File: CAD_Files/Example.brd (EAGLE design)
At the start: 86 x 54 mm, 9 parts, among them IC1 LM555D, Q1 BSS806N

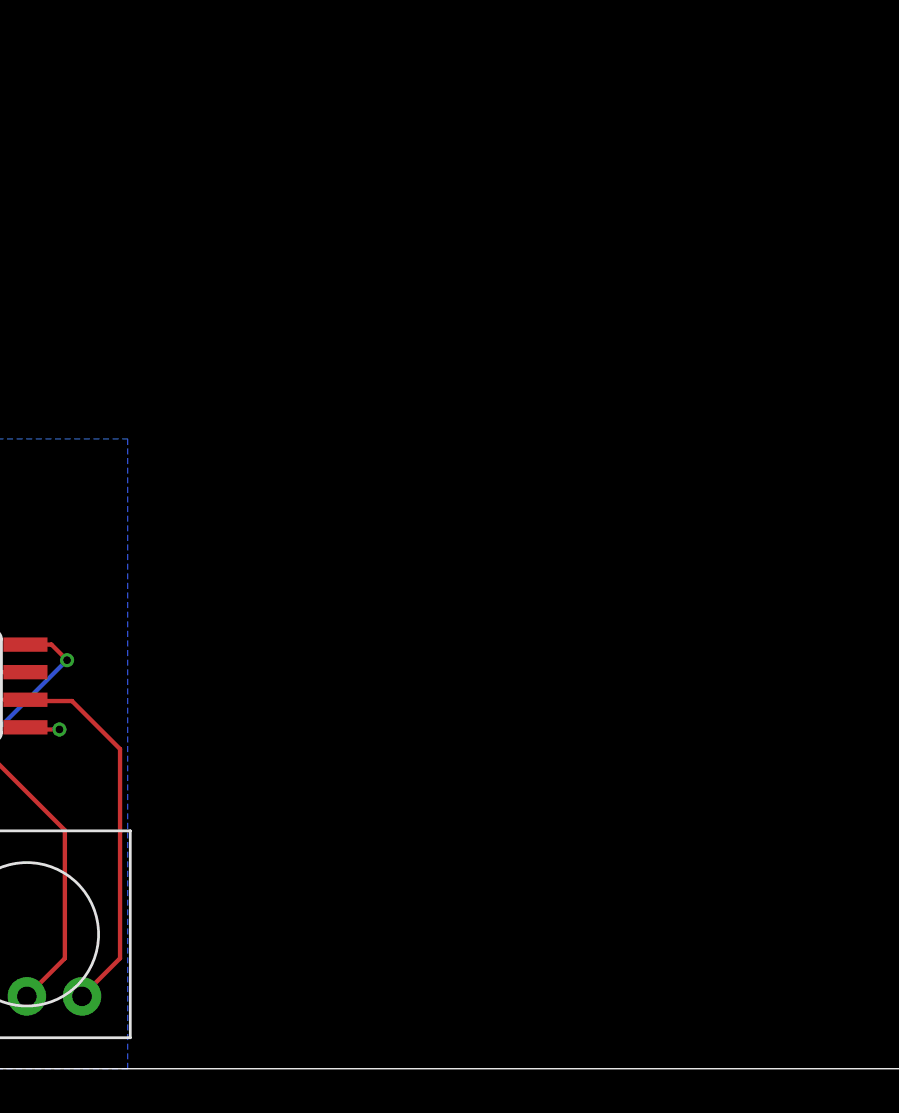
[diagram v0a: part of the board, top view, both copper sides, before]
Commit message: Added picture and silkscreen
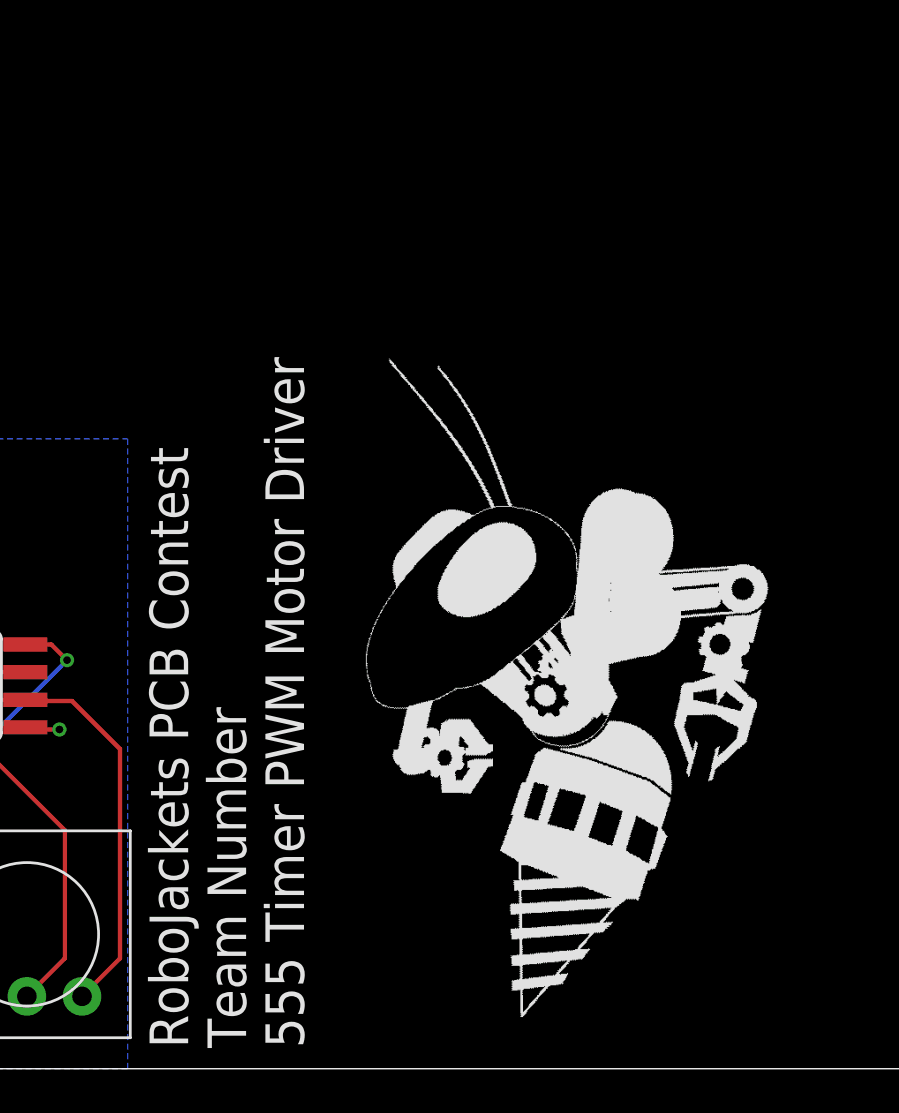
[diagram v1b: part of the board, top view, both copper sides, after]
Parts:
- added U$2: (no value), RoboJackets-Aesthetics:ROBOBUZZ_1.4X
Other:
- board text added: "RoboJackets PCB Contest Team Number 555 Timer PWM Motor Driver"
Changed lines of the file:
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@@
 <setting verticaltext="up"/>
 </settings>
-<grid distance="1" unitdist="mm" unit="mm" style="lines" multiple="1" display="no" altdistance="0.01" altunitdist="mm" altunit="mm"/>
+<grid distance="0.01" unitdist="mm" unit="mm" style="lines" multiple="1" display="no" altdistance="0.01" altunitdist="mm" altunit="mm"/>
 <layers>
 <layer number="1" name="Top" color="4" fill="1" visible="yes" active="yes"/>
@@
 <wire x1="0" y1="54" x2="0" y2="0" width="0" layer="20"/>
 <text x="2.13" y="28.48" size="2.5" layer="21" rot="SR270">ON</text>
+<text x="33.12" y="0.96" size="1.778" layer="21" rot="R90">RoboJackets PCB Contest
+Team Number
+555 Timer PWM Motor Driver</text>
 </plain>
 <attributes>
@@
 </element>
 <element name="U$1" library="Example" package="MFS101D-6-Z" value="MFS101D-6-Z" x="4.91" y="17.97" smashed="yes" rot="R90"/>
+<element name="U$2" library="RoboJackets-Aesthetics" package="ROBOBUZZ_1.4X" value="" x="43.06" y="2.36" smashed="yes"/>
 </elements>
 <signals>
@@
 </signals>
 <mfgpreviewcolors>
-<mfgpreviewcolor name="soldermaskcolor" color="0xC8008000"/>
+<mfgpreviewcolor name="soldermaskcolor" color="0xC8000000"/>
 <mfgpreviewcolor name="silkscreencolor" color="0xFFFEFEFE"/>
 <mfgpreviewcolor name="backgroundcolor" color="0xFF282828"/>
@@
 </drawing>
 <compatibility>
+<note version="6.3" minversion="6.2.2" severity="warning">
+Since Version 6.2.2 text objects can contain more than one line,
+which will not be processed correctly with this version.
+</note>
 <note version="8.2" severity="warning">
 Since Version 8.2, EAGLE supports online libraries. The ids

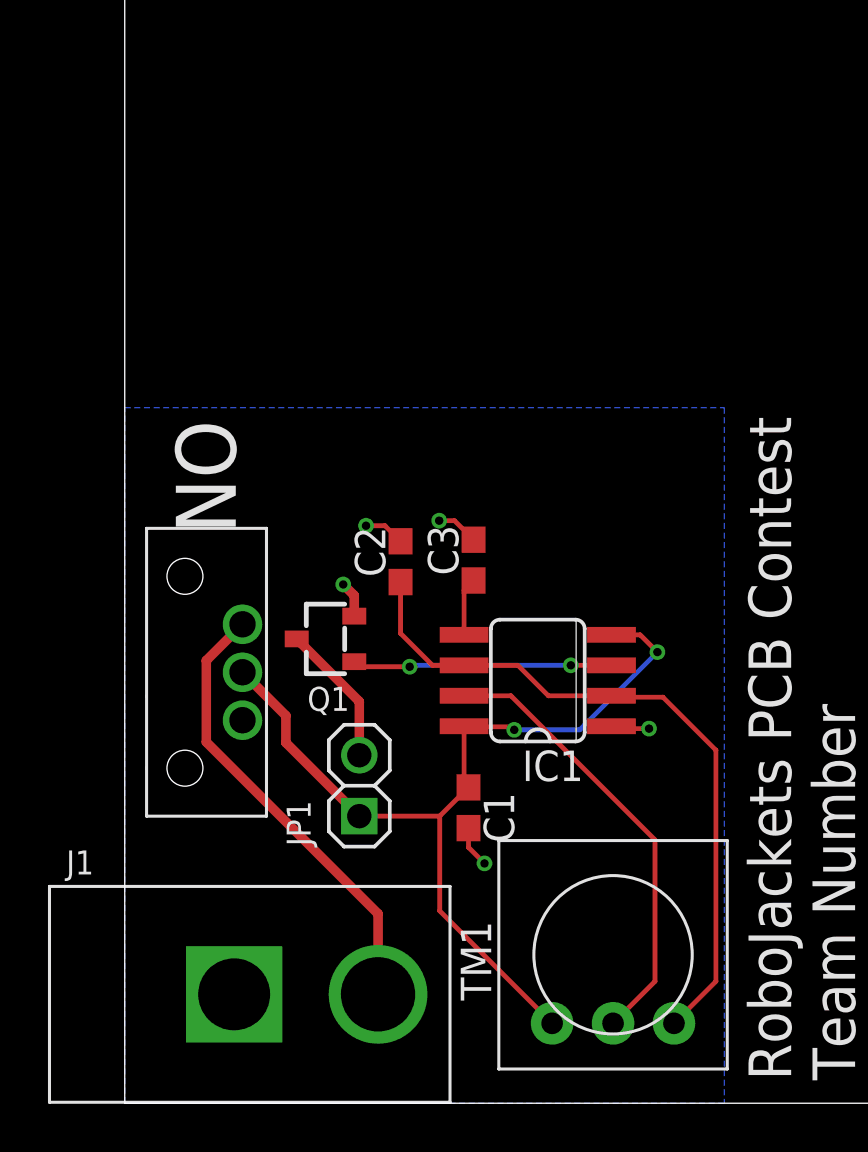
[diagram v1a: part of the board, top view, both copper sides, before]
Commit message: Added decoupling capacitors, fixed Library style guide compliance
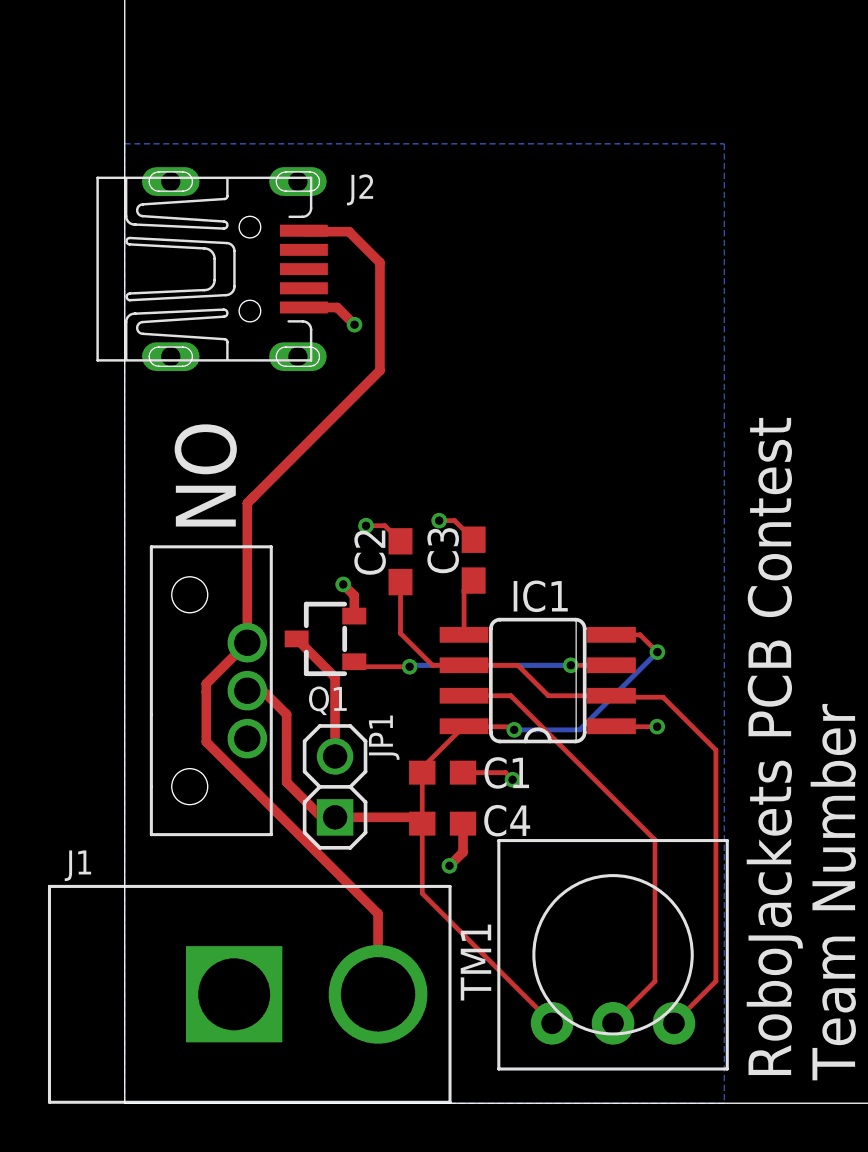
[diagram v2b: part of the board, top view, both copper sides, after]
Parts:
- removed U$1: MFS101D-6-Z, Example:MFS101D-6-Z
- added C4: 10uF, rcl:C0603
- added J2: UX60-MB-5S8, RoboJackets-Connectors:UX60-MB-5S8
- added SW1: MFS101D-6-Z, Example:MFS101D-6-Z
- moved C1 1.82 mm to (13.3, 13.8), turned to 0 degrees
- moved JP1 1.01 mm to (8.77, 13.2)
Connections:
- removed net N$4: J1.P$2, U$1.3
- new net N$5: J1.P$2, J2.1, SW1.3
- net +9V: now also C4.1, SW1.2; no longer U$1.2
- net GND: now also C4.2, J2.5
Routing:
- net N$5: track 0.00 -> 40.2 mm
- net N$4: track 19.0 -> 0.00 mm
- net GND: track 8.34 -> 13.5 mm, vias 5 -> 7

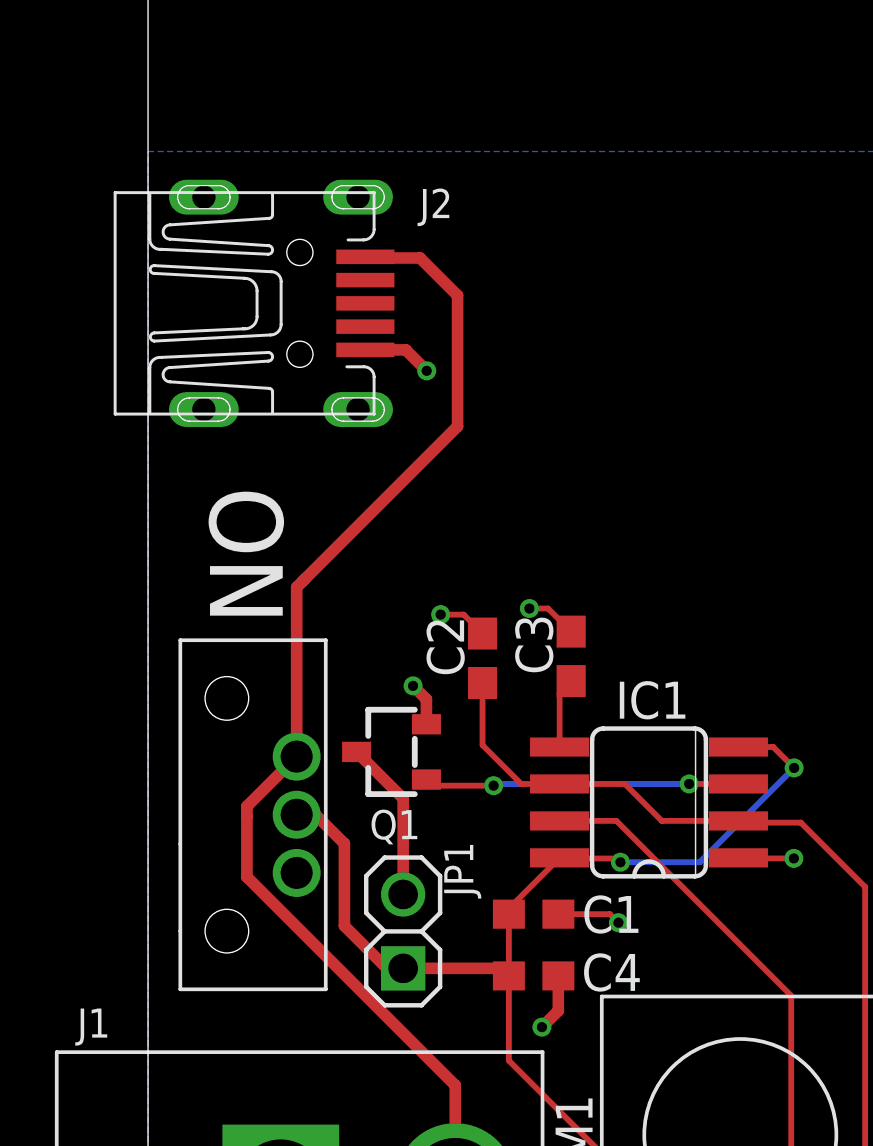
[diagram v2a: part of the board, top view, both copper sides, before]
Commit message: Library edits, power switching transistor, 3d CAD
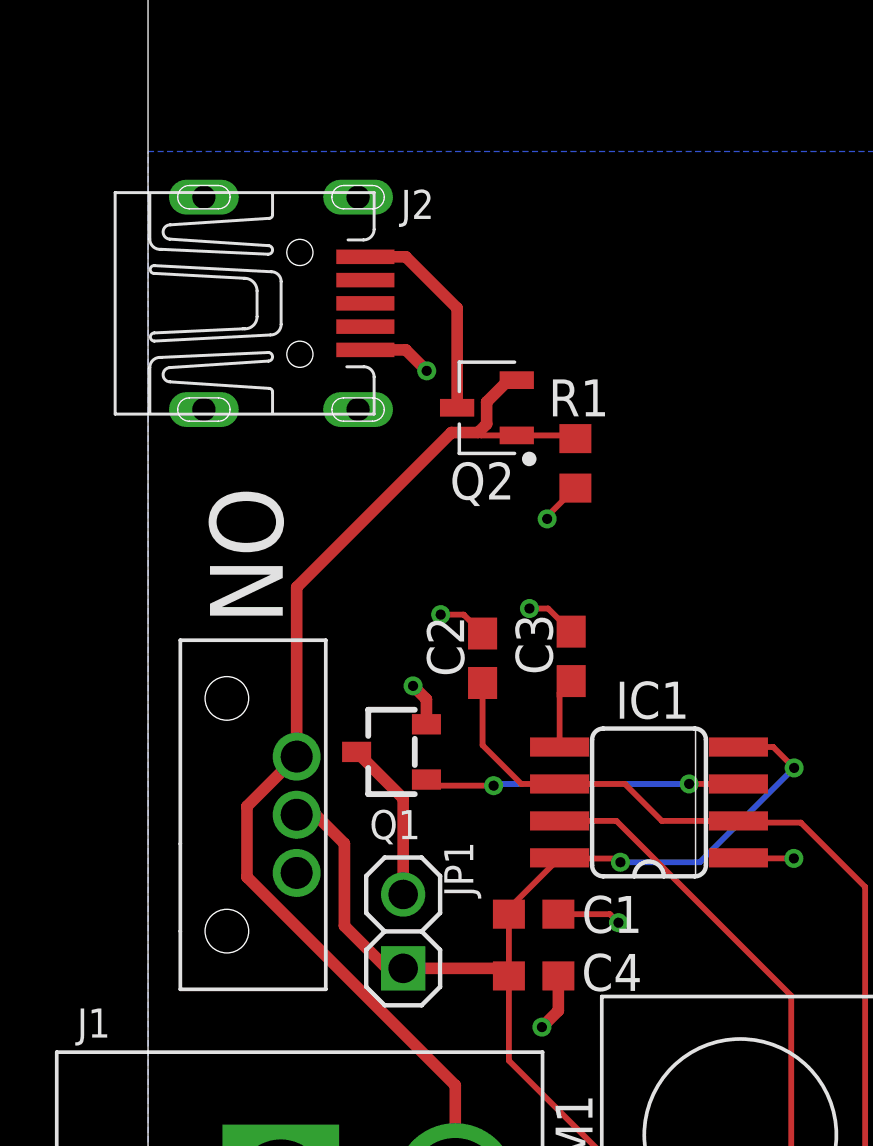
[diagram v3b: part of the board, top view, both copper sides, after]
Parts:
- added Q2: SSM3J356R, Example:SOT95P240X80-3N
- added R1: 10K, rcl:R0603
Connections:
- removed net N$5: J1.P$2, J2.1, SW1.3
- new net N$4: J2.1, Q2.3
- new net N$6: J1.P$2, Q2.1, Q2.2, R1.2, SW1.3
- net GND: now also R1.1
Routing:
- net N$5: track 40.2 -> 0.00 mm
- net N$6: track 0.00 -> 38.5 mm
- net N$4: track 0.00 -> 7.31 mm
- net GND: track 13.5 -> 14.9 mm, vias 7 -> 8
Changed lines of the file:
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@@
 <?xml version="1.0" encoding="utf-8"?>
 <!DOCTYPE eagle SYSTEM "eagle.dtd">
-<eagle version="9.5.2">
+<eagle version="9.6.2">
 <drawing>
 <settings>
@@
 <element name="J2" library="RoboJackets-Connectors" package="UX60-MB-5S8" value="UX60-MB-5S8" x="-1.18" y="34.78" smashed="yes">
 <attribute name="DKPN" value="H2960CT-ND" x="-1.18" y="34.78" size="1.778" layer="27" display="off"/>
-<attribute name="NAME" x="9.33" y="37.71" size="1" layer="25" font="vector"/>
-<attribute name="VALUE" x="-0.18" y="29.78" size="1" layer="27" font="vector" align="top-left"/>
+<attribute name="NAME" x="8.69" y="37.68" size="1" layer="25" font="vector"/>
 </element>
 <element name="C4" library="rcl" library_urn="urn:adsk.eagle:library:334" package="C0603" package3d_urn="urn:adsk.eagle:package:23616/2" value="10uF" x="13.255" y="11.66" smashed="yes">
@@
 <attribute name="SPICEPREFIX" value="C" x="13.255" y="11.66" size="1.778" layer="27" display="off"/>
 </element>
-<element name="SW1" library="Example" package="MFS101D-6-Z" value="MFS101D-6-Z" x="5.11" y="17.2" smashed="yes" rot="R90"/>
+<element name="SW1" library="Example" package="MFS101D-6-Z" value="MFS101D-6-Z" x="5.11" y="17.2" smashed="yes" rot="R90">
+<attribute name="DKPN" value="563-1555-ND" x="5.11" y="17.2" size="1.778" layer="27" rot="R90" display="off"/>
+</element>
+<element name="R1" library="rcl" library_urn="urn:adsk.eagle:library:334" package="R0603" package3d_urn="urn:adsk.eagle:package:23555/3" value="10K" x="14.69" y="29.28" smashed="yes" rot="R90">
+<attribute name="NAME" x="13.765" y="30.895" size="1.27" layer="25"/>
+<attribute name="POPULARITY" value="77" x="14.69" y="29.28" size="1.778" layer="27" rot="R90" display="off"/>
+<attribute name="SPICEPREFIX" value="R" x="14.69" y="29.28" size="1.778" layer="27" rot="R90" display="off"/>
+</element>
+<element name="Q2" library="Example" package="SOT95P240X80-3N" package3d_urn="urn:adsk.eagle:package:24993154/1" value="SSM3J356R" x="11.65" y="31.19" smashed="yes" rot="R180">
+<attribute name="NAME" x="11.49" y="29.3064" size="1.27" layer="25" rot="R180" align="bottom-center"/>
+</element>
 </elements>
 <signals>
@@
 <wire x1="15.877" y1="13.783" x2="16.17" y2="13.49" width="0.2" layer="1"/>
 <via x="16.17" y="13.49" extent="1-16" drill="0.35"/>
+<contactref element="R1" pad="1"/>
+<wire x1="14.69" y1="28.43" x2="13.72" y2="27.46" width="0.2" layer="1"/>
+<wire x1="13.72" y1="27.46" x2="13.72" y2="27.37" width="0.2" layer="1"/>
+<via x="13.72" y="27.37" extent="1-16" drill="0.35"/>
 </signal>
 <signal name="+9V">
@@
 <wire x1="16.239096875" y1="15.569096875" x2="16.11159375" y2="15.6966" width="0.2" layer="1"/>
 <wire x1="16.11159375" y1="15.6966" x2="14.17" y2="15.6966" width="0.2" layer="1"/>
-<wire x1="8.86" y1="12.01" x2="8.77" y2="11.92" width="0.2" layer="1"/>
 <contactref element="C4" pad="1"/>
 <contactref element="SW1" pad="2"/>
@@
 <wire x1="8.77" y1="17.76" x2="8.77" y2="14.46" width="0.4" layer="1"/>
 </signal>
-<signal name="N$5">
+<signal name="N$4">
 <contactref element="J2" pad="1"/>
+<contactref element="Q2" pad="3"/>
+<wire x1="7.47" y1="36.38" x2="8.86" y2="36.38" width="0.4" layer="1"/>
+<wire x1="10.6255" y1="34.6145" x2="10.6255" y2="31.19" width="0.4" layer="1"/>
+<wire x1="8.86" y1="36.38" x2="10.6255" y2="34.6145" width="0.4" layer="1"/>
+</signal>
+<signal name="N$6">
+<contactref element="R1" pad="2"/>
+<contactref element="Q2" pad="1"/>
+<wire x1="14.58" y1="30.24" x2="12.6745" y2="30.24" width="0.2" layer="1"/>
+<wire x1="14.58" y1="30.24" x2="14.69" y2="30.13" width="0.2" layer="1"/>
 <contactref element="J1" pad="P$2"/>
+<contactref element="SW1" pad="3"/>
+<contactref element="Q2" pad="2"/>
 <wire x1="10.562" y1="7.898" x2="10.562" y2="4.54" width="0.4" layer="1"/>
-<wire x1="3.4" y1="15.06" x2="3.4" y2="17.15" width="0.4" layer="1"/>
+<wire x1="3.4" y1="15.06" x2="3.4" y2="17.49" width="0.4" layer="1"/>
 <wire x1="10.562" y1="7.898" x2="3.4" y2="15.06" width="0.4" layer="1"/>
-<wire x1="7.47" y1="36.38" x2="7.51" y2="36.34" width="0.4" layer="1"/>
-<wire x1="7.51" y1="36.34" x2="9.35" y2="36.34" width="0.4" layer="1"/>
-<wire x1="9.35" y1="36.34" x2="10.64" y2="35.05" width="0.4" layer="1"/>
-<wire x1="10.64" y1="35.05" x2="10.64" y2="30.55" width="0.4" layer="1"/>
-<wire x1="10.64" y1="30.55" x2="5.395" y2="25.305" width="0.4" layer="1"/>
-<contactref element="SW1" pad="3"/>
-<wire x1="5.395" y1="25.305" x2="5.31" y2="25.22" width="0.4" layer="1"/>
 <wire x1="5.11" y1="19.2" x2="3.4" y2="17.49" width="0.4" layer="1"/>
-<wire x1="3.4" y1="17.49" x2="3.4" y2="17.15" width="0.4" layer="1"/>
 <wire x1="5.11" y1="19.2" x2="5.11" y2="25.02" width="0.4" layer="1"/>
-<wire x1="5.11" y1="25.02" x2="5.31" y2="25.22" width="0.4" layer="1"/>
+<wire x1="10.43" y1="30.34" x2="11.35" y2="30.34" width="0.4" layer="1"/>
+<wire x1="11.35" y1="30.34" x2="11.64" y2="30.63" width="0.4" layer="1"/>
+<wire x1="11.64" y1="30.63" x2="11.64" y2="31.39" width="0.4" layer="1"/>
+<wire x1="11.64" y1="31.39" x2="12.39" y2="32.14" width="0.4" layer="1"/>
+<wire x1="12.39" y1="32.14" x2="12.6745" y2="32.14" width="0.4" layer="1"/>
+<wire x1="5.11" y1="25.02" x2="10.43" y2="30.34" width="0.4" layer="1"/>
+<wire x1="12.6745" y1="30.24" x2="11.45" y2="30.24" width="0.2" layer="1"/>
+<wire x1="11.45" y1="30.24" x2="11.35" y2="30.34" width="0.2" layer="1"/>
 </signal>
 </signals>
